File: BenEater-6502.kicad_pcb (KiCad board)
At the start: 2 copper layers, 157.5 x 180.3 mm, 108 parts, among them J1 Conn_01x03_Pin, J10 Conn_01x03_Pin, J11 HLT, J12 Conn_01x10, J13 Conn_01x10, J14 Conn_01x10, J2 Conn_01x02, J3 Barrel Jack, J4 Logic Probe, J5 Conn_02x20_Counter_Clockwise, J6 Conn_02x20_Counter_Clockwise, J7 Conn_01x09, J8 Conn_01x09, J9 Conn_01x09, SW1 Step, SW2 Run / Step, SW3 Clk Source, SW4 RESET, SW5 NMI, SW6 Power, U1 LM555, U10 HM62256BLP, U11 W65C22NxP, U12 LCD-16X2, U13 74LS00, U14 W65C22NxP, U15 W65C51NxP, U16 MAX232N, U17 74LS08, U2 LM555, U3 LM555, U4 74LS04, U5 74LS08, U6 74LS32, U7 LM555, U9 28C256, X1 ACO-xxxMHz, Y1 Crystal

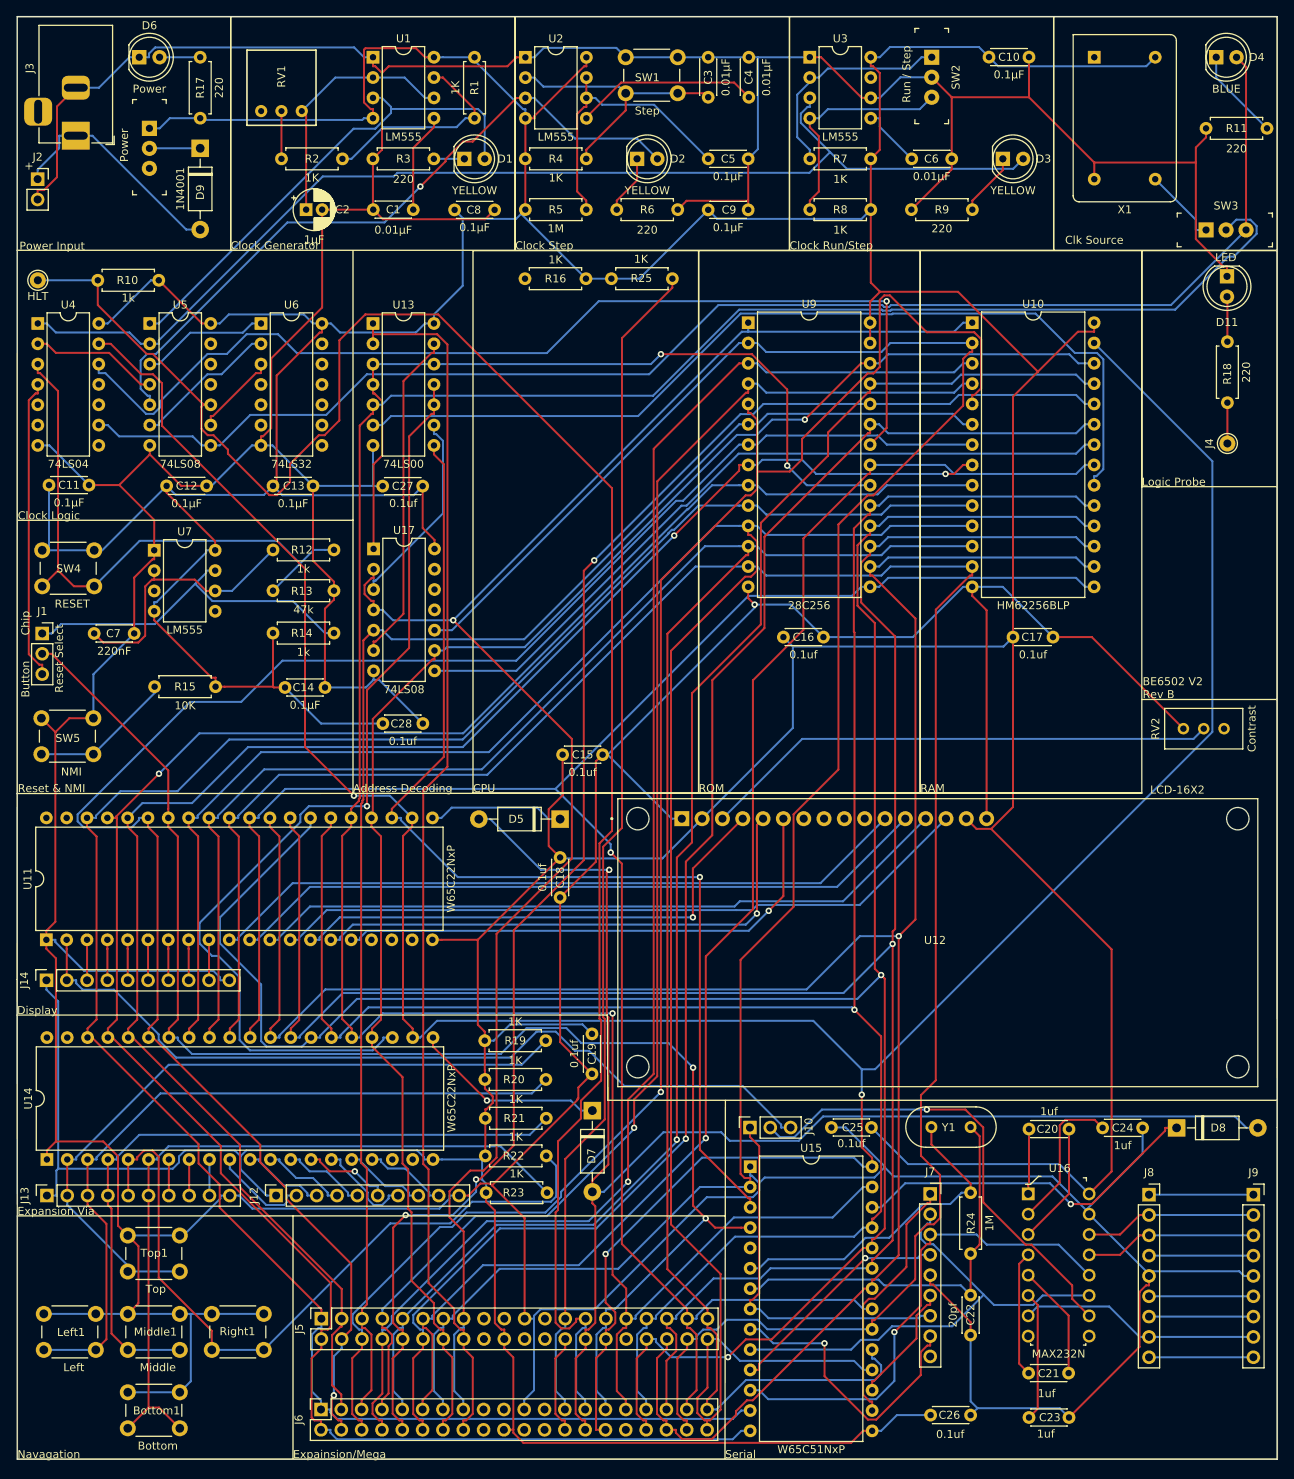
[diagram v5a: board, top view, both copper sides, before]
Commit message: Fixed the addressing Still not fixed
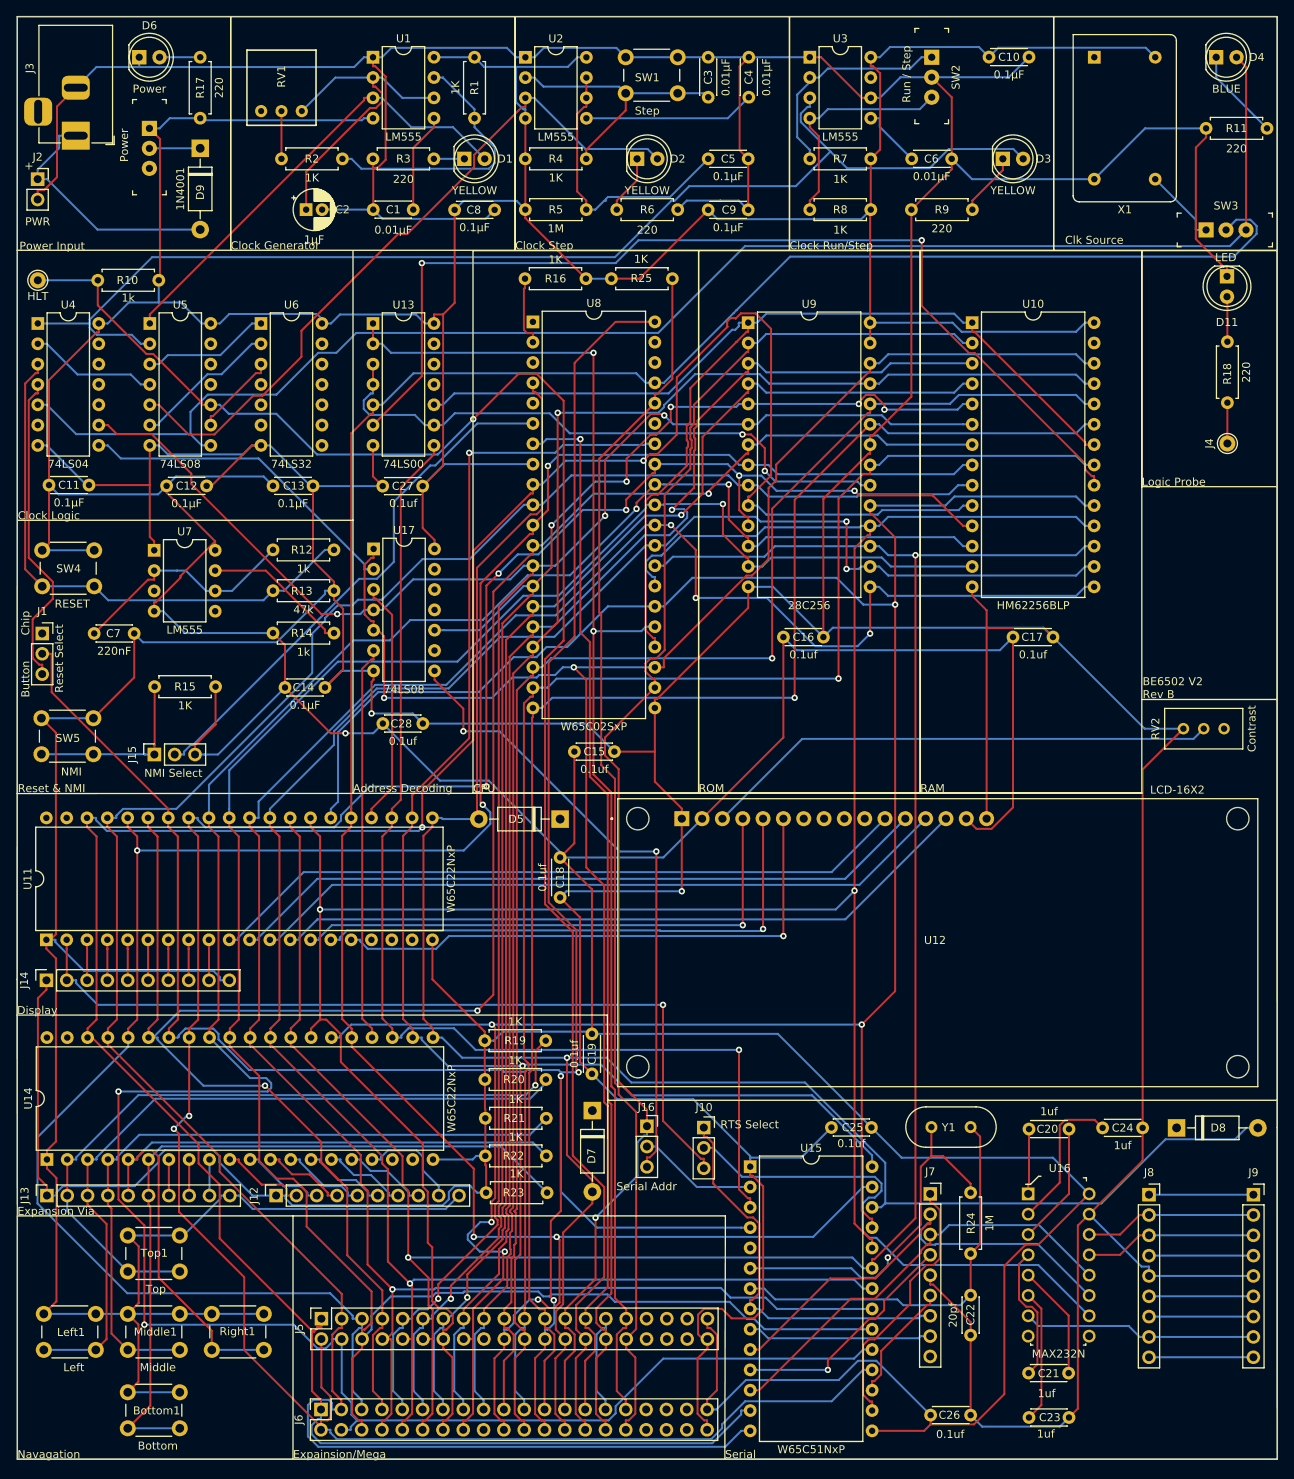
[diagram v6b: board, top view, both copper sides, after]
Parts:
- added J15: NMI Select, Connector_PinSocket_2.54mm:PinSocket_1x03_P2.54mm_Vertical, F.Cu at (32.4, 107.5)
- added J16: Serial Addr, Connector_PinSocket_2.54mm:PinSocket_1x03_P2.54mm_Vertical, F.Cu at (93.9, 153.9)
- added U8: W65C02SxP, Package_DIP:DIP-40_W15.24mm, F.Cu at (79.7, 53.4)
- J10: value Conn_01x03_Pin -> RTS Select
- J2: value Conn_01x02 -> PWR
- R15: value 10K -> 1K
- moved J10 5.77 mm to (101.0, 154.1), turned to 0 degrees
- moved C15 1.52 mm to (84.9, 107.1)
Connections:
- J5 pad 10: /A9 -> /D4
- J5 pad 11: /A10 -> /A5
- J5 pad 12: /A11 -> /D5
- J5 pad 13: /A12 -> /A6
- J5 pad 14: /A13 -> /D6
- J5 pad 15: /A14 -> /A7
- J5 pad 16: /A15 -> /D7
- J5 pad 17: unconnected-(J5-Pin_17-Pad17) -> /A8
- J5 pad 19: unconnected-(J5-Pin_19-Pad19) -> /A9
- J5 pad 2: /A1 -> /D0
- J5 pad 20: +5V -> /CLK
- J5 pad 21: Earth -> /A10
- J5 pad 22: unconnected-(J5-Pin_22-Pad22) -> /R/W
- J5 pad 23: unconnected-(J5-Pin_23-Pad23) -> /A11
- J5 pad 24: unconnected-(J5-Pin_24-Pad24) -> /Reset
- J5 pad 25: /BE -> /A12
- J5 pad 26: /Sync -> /IRQ
- J5 pad 27: /HLT -> /A13
- J5 pad 28: /IRQ -> /HLT
- J5 pad 29: /Reset -> /A14
- J5 pad 3: /A2 -> /A1
- J5 pad 30: /R/W -> /Sync
- J5 pad 31: /CLK -> /A15
- J5 pad 32: unconnected-(J5-Pin_32-Pad32) -> /BE
- J5 pad 33: /D7 -> unconnected-(J5-Pin_33-Pad33)
- J5 pad 34: /D6 -> unconnected-(J5-Pin_34-Pad34)
- J5 pad 35: /D5 -> unconnected-(J5-Pin_35-Pad35)
- J5 pad 36: /D4 -> unconnected-(J5-Pin_36-Pad36)
- J5 pad 37: /D3 -> unconnected-(J5-Pin_37-Pad37)
- J5 pad 38: /D2 -> unconnected-(J5-Pin_38-Pad38)
- J5 pad 39: /D1 -> +5V
- J5 pad 4: /A3 -> /D1
- J5 pad 40: /D0 -> Earth
- J5 pad 5: /A4 -> /A2
- J5 pad 6: /A5 -> /D2
- J5 pad 7: /A6 -> /A3
- J5 pad 8: /A7 -> /D3
- J5 pad 9: /A8 -> /A4
- J6 pad 10: /A9 -> /D4
- J6 pad 11: /A10 -> /A5
- J6 pad 12: /A11 -> /D5
- J6 pad 13: /A12 -> /A6
- J6 pad 14: /A13 -> /D6
- J6 pad 15: /A14 -> /A7
- J6 pad 16: /A15 -> /D7
- J6 pad 17: unconnected-(J6-Pin_17-Pad17) -> /A8
- J6 pad 19: unconnected-(J6-Pin_19-Pad19) -> /A9
- J6 pad 2: /A1 -> /D0
- J6 pad 20: +5V -> /CLK
- J6 pad 21: Earth -> /A10
- J6 pad 22: unconnected-(J6-Pin_22-Pad22) -> /R/W
- J6 pad 23: unconnected-(J6-Pin_23-Pad23) -> /A11
- J6 pad 24: unconnected-(J6-Pin_24-Pad24) -> /Reset
- J6 pad 25: /BE -> /A12
- J6 pad 26: /Sync -> /IRQ
- J6 pad 27: /HLT -> /A13
- J6 pad 28: /IRQ -> /HLT
- J6 pad 29: /Reset -> /A14
- J6 pad 3: /A2 -> /A1
- J6 pad 30: /R/W -> /Sync
- J6 pad 31: /CLK -> /A15
- J6 pad 32: unconnected-(J6-Pin_32-Pad32) -> /BE
- J6 pad 33: /D7 -> unconnected-(J6-Pin_33-Pad33)
- J6 pad 34: /D6 -> unconnected-(J6-Pin_34-Pad34)
- J6 pad 35: /D5 -> unconnected-(J6-Pin_35-Pad35)
- J6 pad 36: /D4 -> unconnected-(J6-Pin_36-Pad36)
- J6 pad 37: /D3 -> unconnected-(J6-Pin_37-Pad37)
- J6 pad 38: /D2 -> unconnected-(J6-Pin_38-Pad38)
- J6 pad 39: /D1 -> +5V
- J6 pad 4: /A3 -> /D1
- J6 pad 40: /D0 -> Earth
- J6 pad 5: /A4 -> /A2
- J6 pad 6: /A5 -> /D2
- J6 pad 7: /A6 -> /A3
- J6 pad 8: /A7 -> /D3
- J6 pad 9: /A8 -> /A4
- U10 pad 22: /RAMOE -> /A14
- U11 pad 21: Net-(D5-K) -> /IRQ
- U11 pad 24: /A13 -> /CS1Via1
- U13 pad 10: /CS2Via2 -> /A14
- U13 pad 11: /CS2Via2 -> (no net)
- U13 pad 12: /ROMCS -> (no net)
- U13 pad 13: Net-(U13-Pad13) -> (no net)
- U13 pad 9: Net-(U13-Pad9) -> /ROMCS
- U14 pad 21: Net-(D7-K) -> /IRQ
- U14 pad 23: /CS2Via2 -> /CS2
- U14 pad 24: /A13 -> /CS1Via2
- U15 pad 2: /A12 -> /CS1Serial
- U15 pad 26: Net-(D8-K) -> /IRQ
- U17 pad 1: /ROMCS -> /A13
- U17 pad 10: /A12 -> /A5
- U17 pad 2: /A14 -> Net-(U17-Pad2)
- U17 pad 3: Net-(U13-Pad9) -> /CS1Via1
- U17 pad 4: /A14 -> /A4
- U17 pad 5: /A4 -> /A13
- U17 pad 6: Net-(U13-Pad13) -> /CS1Via2
- U17 pad 8: /RAMOE -> Net-(J16-Pin_3)
- U17 pad 9: /A13 -> /Control Logic/C1Via1
- U4 pad 12: Net-(U9-~{OE}) -> (no net)
- U4 pad 13: /R/W -> (no net)
- U4 pad 5: (no net) -> Net-(D4-A)
- U4 pad 6: (no net) -> /Clock/~{CLK}
- U4 pad 8: /Clock/~{CLK} -> Net-(U17-Pad2)
- U4 pad 9: Net-(D4-A) -> /A4
- U9 pad 22: Net-(U9-~{OE}) -> Earth
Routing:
- net /R/W: track 360.2 -> 214.1 mm, vias 3 -> 2
- net Net-(U9-~{OE}): track 128.7 -> 0.00 mm, vias 1 -> 0
- net /Sync: track 12.6 -> 134.3 mm, vias 0 -> 1
- net /CS2Via2: track 121.5 -> 0.00 mm, vias 1 -> 0
- net /Reset: track 182.5 -> 301.8 mm, vias 2 -> 3
- net Earth: track 1079.5 -> 1175.0 mm, vias 1 -> 2
- net /RAMOE: track 94.2 -> 0.00 mm
- net /IRQ: track 180.6 -> 265.2 mm
- net /A12: track 259.9 -> 179.3 mm, vias 0 -> 1
- net Net-(J16-Pin_3): track 0.00 -> 79.5 mm, vias 0 -> 2
- net /D7: track 263.5 -> 340.7 mm, vias 1 -> 5
- net /A0: track 271.5 -> 339.4 mm, vias 0 -> 2
- net Net-(J15-Pin_2): track 0.00 -> 66.5 mm
- net /A4: track 187.3 -> 250.8 mm, vias 0 -> 4
- net /A14: track 212.3 -> 154.9 mm, vias 1 -> 0
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
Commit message: updated plots
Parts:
- added ?: , , F.Cu at (167.7, 191.2)
- added ?: , , F.Cu at (167.9, 19.3)
- added ?: , , F.Cu at (17.8, 35.7)
- added ?: , , F.Cu at (17.9, 191.1)
- J2: value PWR -> Conn_01x02
- moved D4 7.19 mm to (165.4, 27.5)
- moved R11 5.38 mm to (170.2, 34.5)
- moved J2 4.96 mm to (22.6, 36.8)
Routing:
- net /A14: track 154.9 -> 366.9 mm, vias 0 -> 2
- net /R/W: track 214.1 -> 421.7 mm, vias 2 -> 7
- net Net-(J1-Pin_1): track 18.3 -> 50.8 mm, vias 0 -> 1
- net /CLK: track 322.8 -> 313.5 mm, vias 3 -> 4
- net Net-(D4-A): track 190.0 -> 182.7 mm
- net Net-(D9-A): track 31.6 -> 24.3 mm
- net Earth: track 1175.0 -> 1170.2 mm
- net Net-(D4-K): track 11.5 -> 9.37 mm
- net /BE: track 151.4 -> 152.6 mm
- net Net-(SW3-A): track 9.73 -> 8.98 mm
- net /A7: track 182.2 -> 181.7 mm

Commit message: It works
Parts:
- removed ? (x4): , 
- added BottomLeft: MountingHole_2.7mm, MountingHole:MountingHole_2.7mm, F.Cu at (17.5, 190.7)
- added BottomRight: MountingHole_2.7mm, MountingHole:MountingHole_2.7mm, F.Cu at (167.7, 191.2)
- added TopLeft: MountingHole_2.7mm, MountingHole:MountingHole_2.7mm, F.Cu at (17.8, 35.7)
- added TopRight: MountingHole_2.7mm, MountingHole:MountingHole_2.7mm, F.Cu at (167.9, 19.3)
- moved D8 73.0 mm to (87.1, 151.9), turned to -90 degrees
- moved C26 41.1 mm to (149.2, 154.0), turned to 180 degrees
- moved C25 39.8 mm to (132.2, 192.6), turned to 90 degrees
- moved D7 35.0 mm to (122.1, 153.8), turned to 180 degrees
- moved C24 28.5 mm to (136.6, 178.8), turned to -90 degrees
- moved C20 16.6 mm to (136.6, 167.4), turned to 90 degrees
- moved C21 14.0 mm to (136.7, 175.1), turned to 90 degrees
- moved C22 11.0 mm to (132.7, 164.1), turned to 180 degrees
- moved R24 10.8 mm to (134.4, 159.1), turned to 180 degrees
- moved D5 10.3 mm to (72.8, 115.4), turned to 0 degrees
- moved J7 9.50 mm to (127.3, 171.7)
- moved J5 7.93 mm to (53.1, 170.1)
- moved C16 3.96 mm to (111.5, 96.7), turned to 180 degrees
- moved C17 3.75 mm to (139.5, 96.5), turned to 180 degrees
- moved C23 2.78 mm to (141.5, 187.6), turned to 180 degrees
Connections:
- U11 pad 21: /IRQ -> Net-(D5-K)
- U14 pad 21: /IRQ -> Net-(D8-K)
- U15 pad 26: /IRQ -> Net-(D7-K)
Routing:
- net /R/W: track 421.7 -> 288.1 mm, vias 7 -> 3
- net /A14: track 366.9 -> 242.6 mm, vias 2 -> 1
- net /IRQ: track 265.2 -> 173.3 mm, vias 1 -> 0
- net +5V: track 1001.4 -> 1047.6 mm
- net /HLT: track 218.1 -> 261.4 mm, vias 1 -> 2
- net /RAMCS: track 126.6 -> 93.3 mm, vias 2 -> 0
- net /BE: track 152.6 -> 185.1 mm, vias 0 -> 3
- net /ROMCS: track 76.4 -> 106.8 mm, vias 2 -> 3
- net /A12: track 179.2 -> 207.9 mm, vias 1 -> 2
- net /D2: track 277.2 -> 305.1 mm
- net Net-(D8-K): track 0.00 -> 24.5 mm
- net /A1: track 285.1 -> 309.3 mm, vias 0 -> 3
- net /D4: track 272.8 -> 297.0 mm, vias 3 -> 0
- net /CLK: track 313.5 -> 335.0 mm, vias 4 -> 2
- net /A4: track 250.4 -> 271.7 mm, vias 4 -> 3
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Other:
- board text added: "BE6502 V2 Rev C"
- board text removed: "BE6502 V2 Rev B"
